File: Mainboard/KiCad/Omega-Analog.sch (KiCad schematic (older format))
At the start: 97 parts, among them J3 Audio, J6 Cassette, Q1 PN2907A, U48 MCP601, U49 LM311

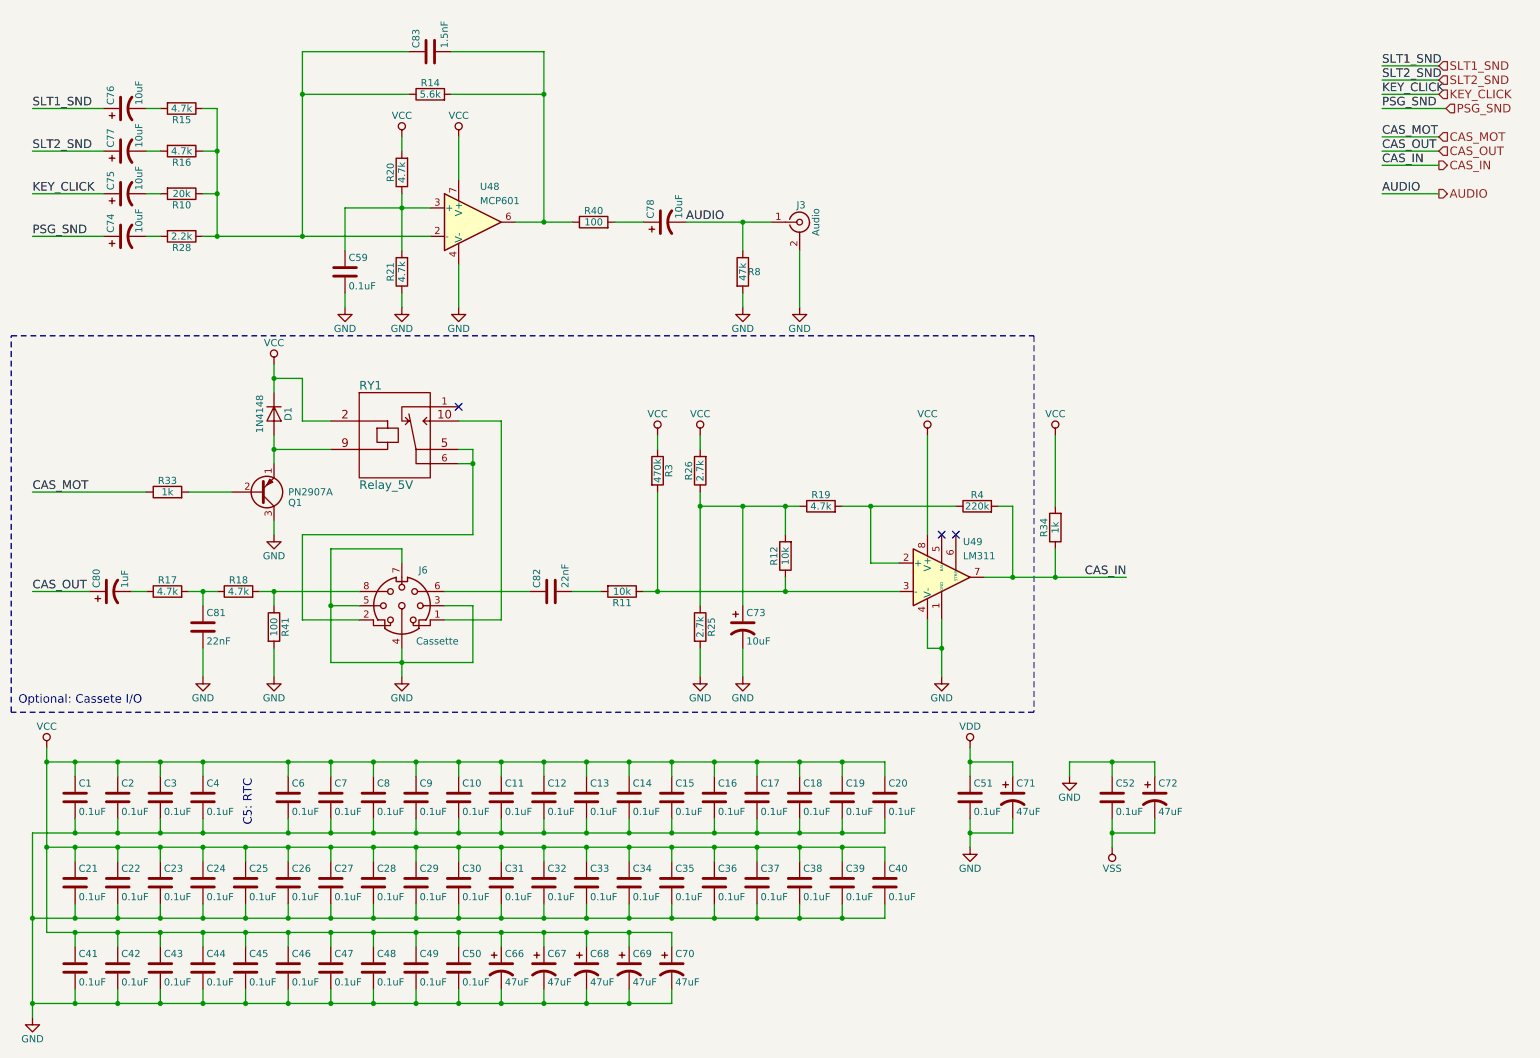
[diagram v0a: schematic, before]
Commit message: Mainboard: Replace RGB and Cassette connectors with DIN8
Signed-off-by: Sergey Kiselev <skiselev@gmail.com>
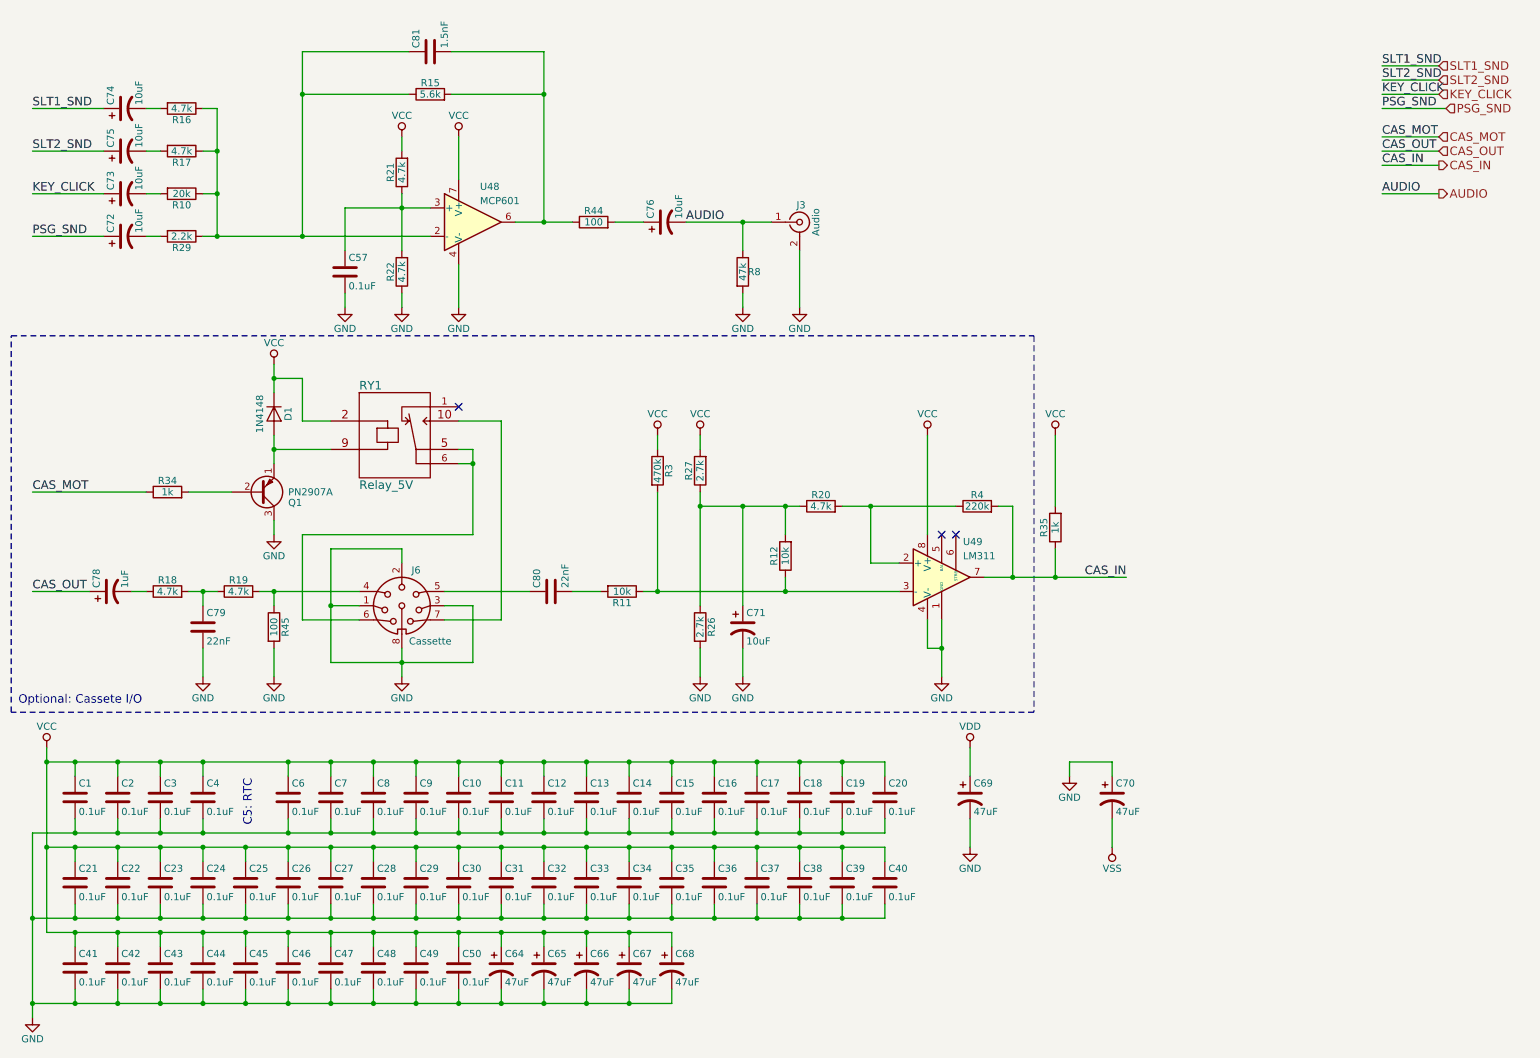
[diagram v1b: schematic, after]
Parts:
- removed C51, C52: 0.1uF, My_Components:Cap_Cer_508, symbol Device:C
- removed J6: Cassette, My_Components:Conn_Mini_DIN_8pin, symbol Connector:Mini-DIN-8
- added J6: Cassette, My_Components:Conn_DIN_8pin, symbol Connector:DIN-8
- renumbered C59 to C57, C66 to C64, C67 to C65, C68 to C66, C69 to C67, C70 to C68, C71 to C69, C72 to C70, C73 to C71, C74 to C72, C75 to C73, C76 to C74, C77 to C75, C78 to C76, C80 to C78, C81 to C79, C82 to C80, C83 to C81, R14 to R15, R15 to R16, R16 to R17, R17 to R18, R18 to R19, R19 to R20, R20 to R21, R21 to R22, R25 to R26, R26 to R27, R28 to R29, R33 to R34, R34 to R35, R40 to R44, R41 to R45
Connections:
- net GND: now also J6.1, J6.2, J6.3, J6.8
- net at C80.1: now also J6.5
- net at R19.2, R45.1: now also J6.4
- net at RY1.10: now also J6.7
- net at RY1.5, RY1.6: now also J6.6
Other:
- moved on the sheet: C69, C70
